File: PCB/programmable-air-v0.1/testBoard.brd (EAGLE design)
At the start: 28.1 x 28.1 mm, 1 part

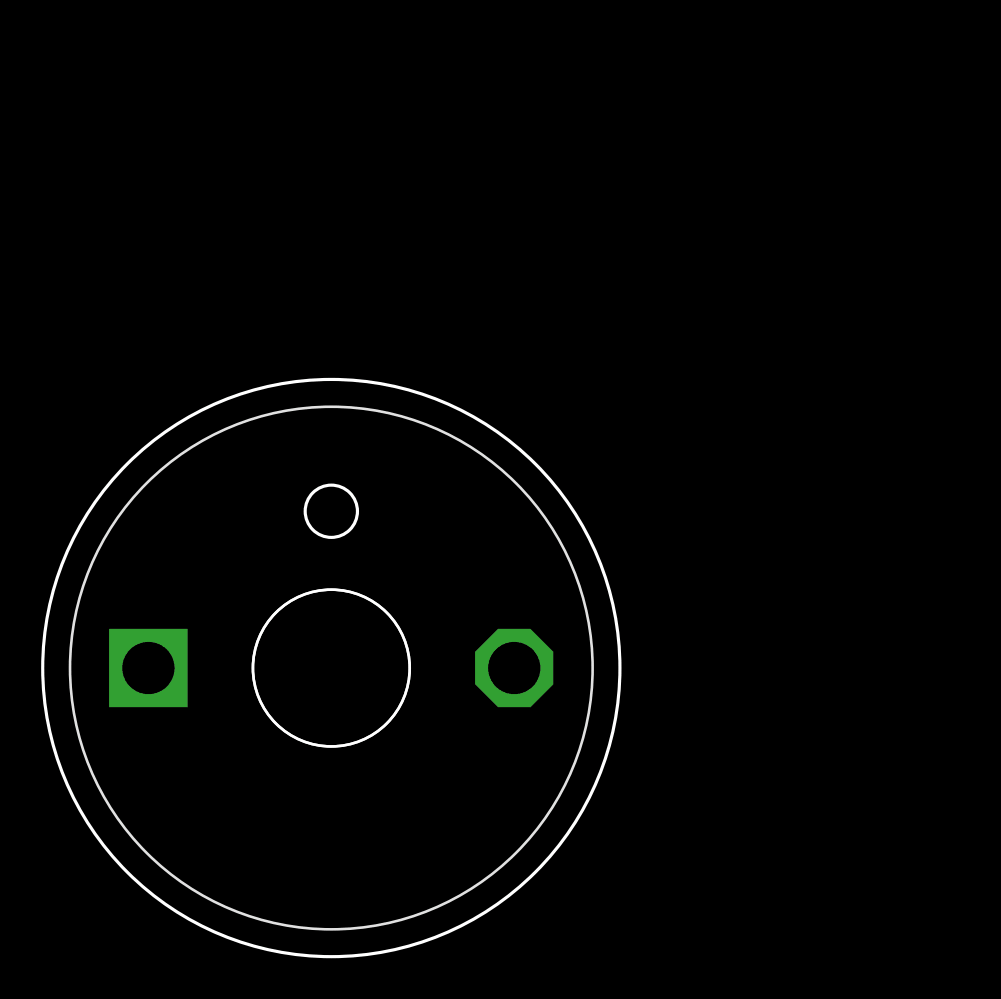
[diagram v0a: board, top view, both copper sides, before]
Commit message: Made pump nad valve PCB library. PCB Mockup made. Added arduino nano footprint.
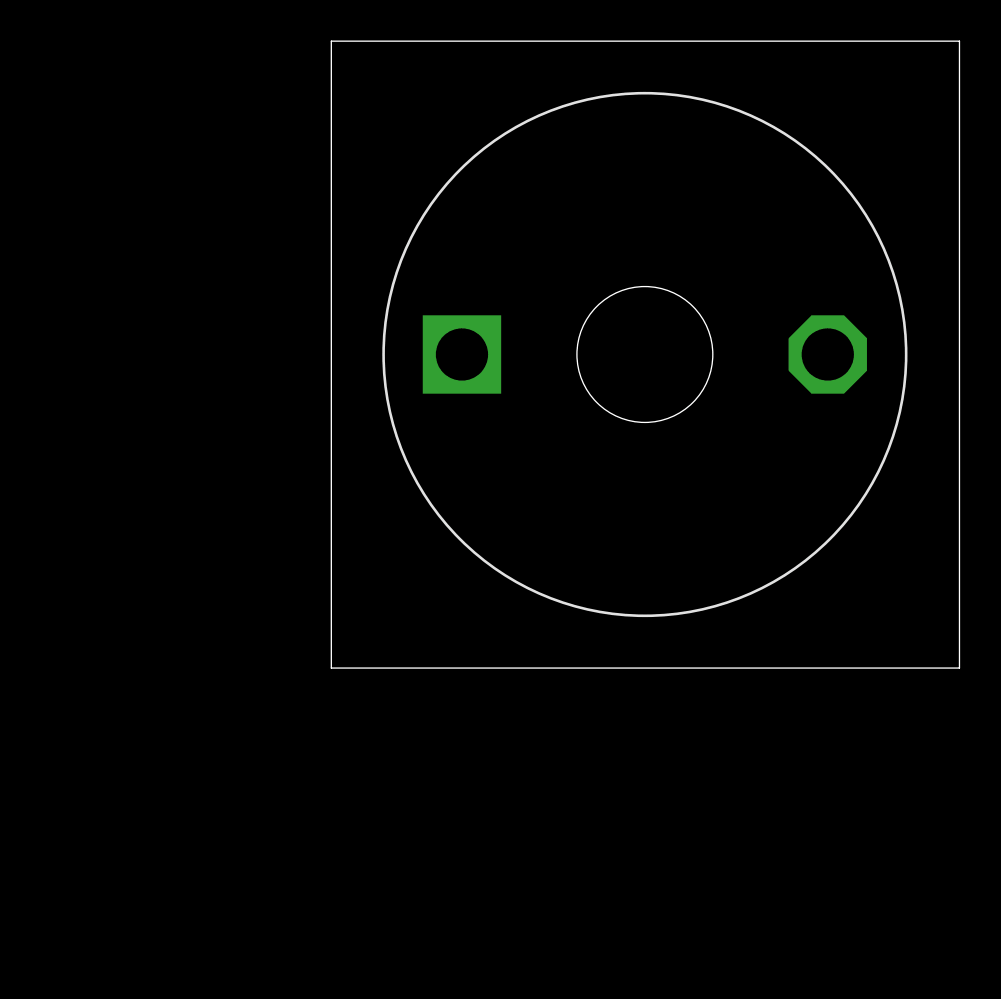
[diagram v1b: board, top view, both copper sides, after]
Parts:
- removed E$1: (no value), programmable-air-components:A5F083
- added U$1: AIYIMA-PUMP-A5F083, programmable-air-components:A5F083
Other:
- board size 28.1 x 28.1 mm -> 30.5 x 30.5 mm
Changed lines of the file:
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@@
 <settings>
 <setting alwaysvectorfont="no"/>
-<setting keepoldvectorfont="yes"/>
 <setting verticaltext="up"/>
 </settings>
@@
 <layers>
 <layer number="1" name="Top" color="4" fill="1" visible="yes" active="yes"/>
-<layer number="2" name="Route2" color="1" fill="3" visible="no" active="no"/>
-<layer number="3" name="Route3" color="4" fill="3" visible="no" active="no"/>
-<layer number="4" name="Route4" color="1" fill="4" visible="no" active="no"/>
-<layer number="5" name="Route5" color="4" fill="4" visible="no" active="no"/>
-<layer number="6" name="Route6" color="1" fill="8" visible="no" active="no"/>
-<layer number="7" name="Route7" color="4" fill="8" visible="no" active="no"/>
-<layer number="8" name="Route8" color="1" fill="2" visible="no" active="no"/>
-<layer number="9" name="Route9" color="4" fill="2" visible="no" active="no"/>
-<layer number="10" name="Route10" color="1" fill="7" visible="no" active="no"/>
-<layer number="11" name="Route11" color="4" fill="7" visible="no" active="no"/>
-<layer number="12" name="Route12" color="1" fill="5" visible="no" active="no"/>
-<layer number="13" name="Route13" color="4" fill="5" visible="no" active="no"/>
-<layer number="14" name="Route14" color="1" fill="6" visible="no" active="no"/>
-<layer number="15" name="Route15" color="4" fill="6" visible="no" active="no"/>
 <layer number="16" name="Bottom" color="1" fill="1" visible="yes" active="yes"/>
 <layer number="17" name="Pads" color="2" fill="1" visible="yes" active="yes"/>
 <layer number="18" name="Vias" color="2" fill="1" visible="yes" active="yes"/>
 <layer number="19" name="Unrouted" color="6" fill="1" visible="yes" active="yes"/>
-<layer number="20" name="Dimension" color="15" fill="1" visible="yes" active="yes"/>
+<layer number="20" name="Dimension" color="24" fill="1" visible="yes" active="yes"/>
 <layer number="21" name="tPlace" color="7" fill="1" visible="yes" active="yes"/>
 <layer number="22" name="bPlace" color="7" fill="1" visible="yes" active="yes"/>
@@
 <layer number="43" name="vRestrict" color="2" fill="10" visible="yes" active="yes"/>
 <layer number="44" name="Drills" color="7" fill="1" visible="no" active="yes"/>
-<layer number="45" name="Holes" color="7" fill="1" visible="yes" active="yes"/>
+<layer number="45" name="Holes" color="7" fill="1" visible="no" active="yes"/>
 <layer number="46" name="Milling" color="3" fill="1" visible="no" active="yes"/>
 <layer number="47" name="Measures" color="7" fill="1" visible="no" active="yes"/>
@@
 <layer number="51" name="tDocu" color="7" fill="1" visible="yes" active="yes"/>
 <layer number="52" name="bDocu" color="7" fill="1" visible="yes" active="yes"/>
+<layer number="88" name="SimResults" color="9" fill="1" visible="no" active="no"/>
+<layer number="89" name="SimProbes" color="9" fill="1" visible="no" active="no"/>
 <layer number="90" name="Modules" color="5" fill="1" visible="no" active="no"/>
 <layer number="91" name="Nets" color="2" fill="1" visible="no" active="no"/>
@@
 <board>
 <plain>
-<circle x="0" y="0" radius="14.02760625" width="0.1524" layer="20"/>
-<hole x="0" y="0" drill="7.62"/>
-<circle x="0" y="7.62" radius="1.27" width="0.1524" layer="20"/>
+<wire x1="0" y1="0" x2="30.531" y2="0" width="0" layer="20"/>
+<wire x1="30.531" y1="0" x2="30.531" y2="30.47" width="0" layer="20"/>
+<wire x1="30.531" y1="30.47" x2="0" y2="30.47" width="0" layer="20"/>
+<wire x1="0" y1="30.47" x2="0" y2="0" width="0" layer="20"/>
 </plain>
 <attributes>
@@
 </autorouter>
 <elements>
-<element name="E$1" library="programmable-air-components" package="A5F083" value="" x="0" y="0"/>
+<element name="U$1" library="programmable-air-components" package="A5F083" value="AIYIMA-PUMP-A5F083" x="15.24" y="15.24"/>
 </elements>
 <signals>
